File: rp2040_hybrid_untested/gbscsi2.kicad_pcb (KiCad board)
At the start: 4 copper layers, 69.5 x 93.5 mm, 143 parts, among them J1 USB_DATA, J2 TF003, J3 Conn_01x02, J4 Conn_01x04, J5 SCSI_50-2P_2mm, J6 SCSI_50P_2.54mm, J7 Conn_01x04, Q1 AO3401A, Q10 AO3401A, Q11 AO3401A, Q12 AO3401A, Q13 AO3401A, Q14 AO3401A, Q15 AO3401A, Q16 AO3401A, Q17 AO3401A, Q18 AO3401A, Q2 AO3401A, Q3 AO3401A, Q4 AO3401A, Q5 AO3401A, Q6 AO3401A, Q7 AO3401A, Q8 AO3401A, Q9 AO3401A, SW1 SW_DIP_x04, U1 RP2040, U10 W25Q128JVS, U2 74LVT245, U3 74LVT245, U4 74AHCT1G125, U5 74LVT125, U6 74LVT125, U7 AZ1117-2.85, U8 AP62250WU, U9 USB TVS, Y1 12MHz

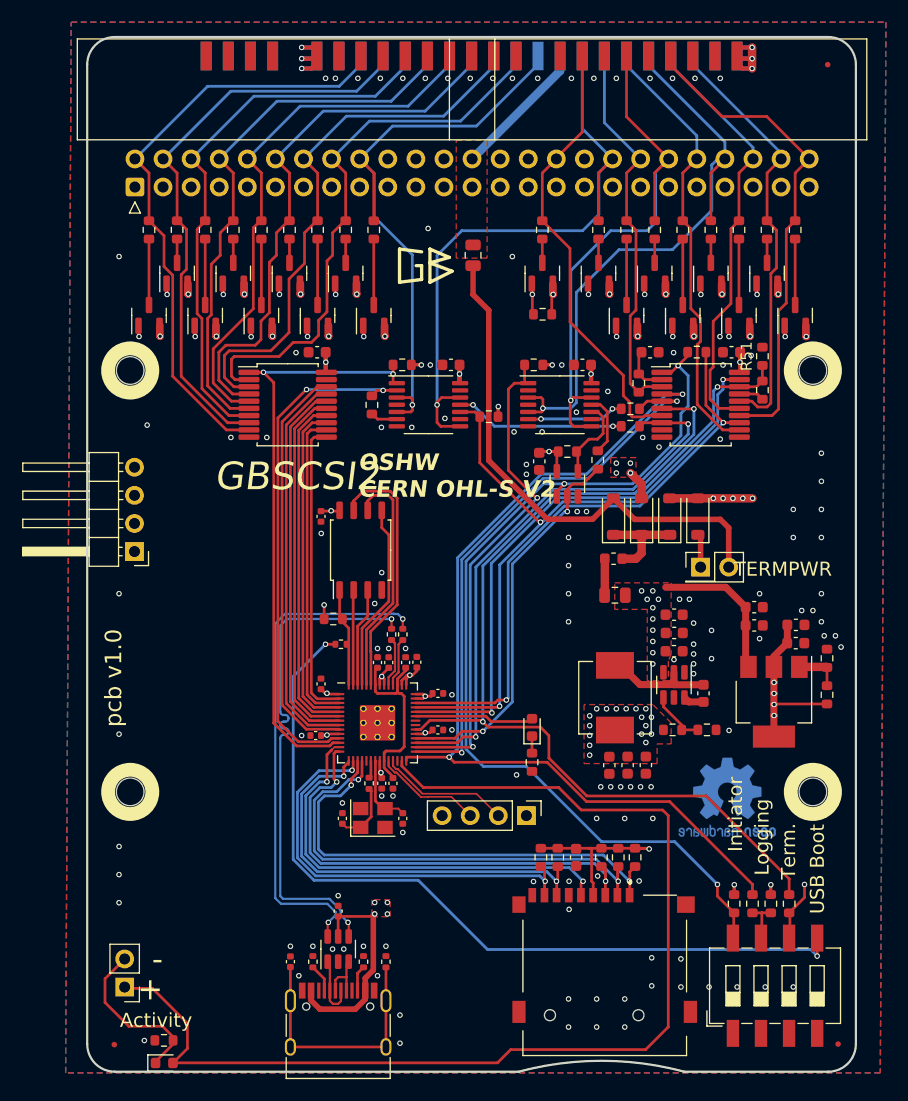
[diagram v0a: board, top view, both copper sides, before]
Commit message: Corrected wrong keying on 2.5" connector
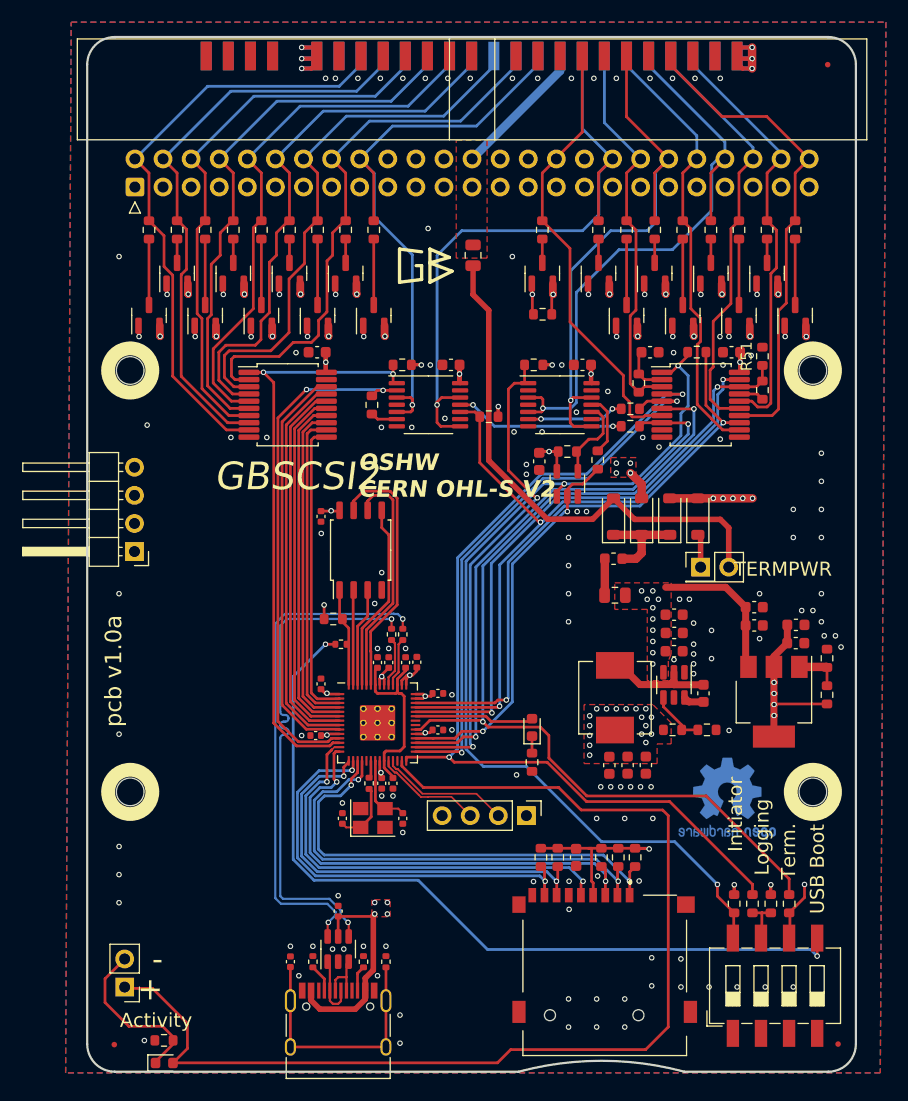
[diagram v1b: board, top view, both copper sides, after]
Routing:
- net GND: vias 134 -> 133
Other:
- board text added: "pcb v1.0a"
- board text removed: "pcb v1.0"
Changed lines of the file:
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@@
     (pad "16" smd rect (at -2.085 0 90) (size 2.58 1) (layers "B.Cu" "B.Paste" "B.Mask")
       (net 22 "/~{SCSI_SD5}") (pinfunction "Pin_16") (pintype "passive"))
-    (pad "17" smd rect (at -2.085 2 90) (size 2.58 1) (layers "F.Cu" "F.Paste" "F.Mask")
-      (net 1 "GND") (pinfunction "Pin_17") (pintype "passive"))
     (pad "18" smd rect (at -2.085 2 90) (size 2.58 1) (layers "B.Cu" "B.Paste" "B.Mask")
       (net 23 "/~{SCSI_SD6}") (pinfunction "Pin_18") (pintype "passive"))
@@
     (pad "20" smd rect (at -2.085 4 90) (size 2.58 1) (layers "B.Cu" "B.Paste" "B.Mask")
       (net 24 "/~{SCSI_SD7}") (pinfunction "Pin_20") (pintype "passive"))
+    (pad "21" smd rect (at -2.085 6 90) (size 2.58 1) (layers "F.Cu" "F.Paste" "F.Mask"))
     (pad "22" smd rect (at -2.085 6 90) (size 2.58 1) (layers "B.Cu" "B.Paste" "B.Mask")
       (net 25 "/~{SCSI_SDP}") (pinfunction "Pin_22") (pintype "passive"))
@@
   (gr_line (start 42.8 43.65) (end 107.3 43.65)
     (stroke (width 0.2) (type solid)) (layer "Edge.Cuts"))
-  (gr_text "pcb v1.0" (at 43.561 106.045 90) (layer "F.SilkS")
+  (gr_text "pcb v1.0a" (at 43.561 106.045 90) (layer "F.SilkS")
     (effects (font (face "OCR A Extended") (size 1.5 1.5) (thickness 0.15)) (justify left bottom))
-    (render_cache "pcb v1.0" 90
+    (render_cache "pcb v1.0a" 90
       (polygon
         (pts
@@
         )
       )
+      (polygon
+        (pts
+          (xy 43.235452 94.82011)          (xy 43.251515 94.824581)          (xy 43.266204 94.832303)          (xy 43.27793 94.841728)
+          (xy 43.281087 94.844877)          (xy 43.290794 94.856553)          (xy 43.298968 94.871013)          (xy 43.304029 94.886664)
+          (xy 43.305902 94.901335)          (xy 43.306 94.905694)          (xy 43.304702 94.921357)          (xy 43.30081 94.935968)
+          (xy 43.294324 94.949527)          (xy 43.285243 94.962034)          (xy 43.278889 94.968709)          (xy 43.266306 94.978701)
+          (xy 43.252602 94.98624)          (xy 43.237776 94.991324)          (xy 43.221827 94.993953)          (xy 43.21221 94.994354)
+          (xy 43.306 95.140533)          (xy 43.306 95.433258)          (xy 43.305346 95.453439)          (xy 43.303385 95.47304)
+          (xy 43.300117 95.492062)          (xy 43.295541 95.510504)          (xy 43.289658 95.528366)          (xy 43.282468 95.545649)
+          (xy 43.27397 95.562352)          (xy 43.264165 95.578476)          (xy 43.253053 95.59402)          (xy 43.240634 95.608984)
+          (xy 43.231628 95.618639)          (xy 43.217399 95.632257)          (xy 43.202605 95.644536)          (xy 43.187243 95.655476)
+          (xy 43.171315 95.665075)          (xy 43.15482 95.673336)          (xy 43.137758 95.680257)          (xy 43.12013 95.685838)
+          (xy 43.101935 95.69008)          (xy 43.083173 95.692982)          (xy 43.063844 95.694545)          (xy 43.050644 95.694842)
+          (xy 42.951725 95.694842)          (xy 42.932212 95.69417)          (xy 42.91324 95.692151)          (xy 42.894809 95.688786)
+          (xy 42.876918 95.684075)          (xy 42.859569 95.678018)          (xy 42.842761 95.670615)          (xy 42.826493 95.661866)
+          (xy 42.810767 95.651772)          (xy 42.795581 95.640331)          (xy 42.780937 95.627545)          (xy 42.771474 95.618272)
+          (xy 42.758052 95.603573)          (xy 42.74595 95.588326)          (xy 42.735169 95.572532)          (xy 42.725707 95.556191)
+          (xy 42.717566 95.539302)          (xy 42.710745 95.521866)          (xy 42.705244 95.503882)          (xy 42.701063 95.485351)
+          (xy 42.698203 95.466272)          (xy 42.696663 95.446646)          (xy 42.696369 95.433258)          (xy 42.860501 95.433258)
+          (xy 42.861763 95.448458)          (xy 42.86555 95.462641)          (xy 42.872968 95.477604)          (xy 42.882165 95.489608)
+          (xy 42.886879 95.494441)          (xy 42.898945 95.504291)          (xy 42.912063 95.511722)          (xy 42.926234 95.516733)
+          (xy 42.941456 95.519325)          (xy 42.950626 95.51972)          (xy 43.051743 95.51972)          (xy 43.067173 95.518493)
+          (xy 43.081726 95.514812)          (xy 43.095403 95.508676)          (xy 43.108203 95.500086)          (xy 43.115124 95.494075)
+          (xy 43.125545 95.482274)          (xy 43.133406 95.469632)          (xy 43.139257 95.454153)          (xy 43.141764 95.437575)
+          (xy 43.141868 95.433258)          (xy 43.141868 95.188893)          (xy 43.048079 95.000216)          (xy 42.961983 95.005345)
+          (xy 42.946274 95.006594)          (xy 42.931569 95.009518)          (xy 42.915684 95.015045)          (xy 42.901166 95.022852)
+          (xy 42.88981 95.031357)          (xy 42.878389 95.042639)          (xy 42.869774 95.055009)          (xy 42.863964 95.068465)
+          (xy 42.860959 95.083008)          (xy 42.860501 95.091807)          (xy 42.860501 95.433258)          (xy 42.696369 95.433258)
+          (xy 42.696369 95.094005)          (xy 42.696209 95.078549)          (xy 42.695806 95.062508)          (xy 42.695265 95.046889)
+          (xy 42.694544 95.029544)          (xy 42.693805 95.013771)          (xy 42.571439 95.015969)          (xy 42.556257 95.017179)
+          (xy 42.540194 95.021524)          (xy 42.525506 95.029029)          (xy 42.51378 95.038187)          (xy 42.510623 95.041249)
+          (xy 42.500773 95.052817)          (xy 42.492478 95.067282)          (xy 42.487343 95.083076)          (xy 42.485442 95.097985)
+          (xy 42.485344 95.102431)          (xy 42.485344 95.43106)          (xy 42.484186 95.445866)          (xy 42.480031 95.461758)
+          (xy 42.472852 95.476549)          (xy 42.464092 95.488591)          (xy 42.461163 95.491877)          (xy 42.450004 95.501869)
+          (xy 42.436219 95.510284)          (xy 42.421336 95.515494)          (xy 42.405353 95.517497)          (xy 42.403278 95.517522)
+          (xy 42.386883 95.515942)          (xy 42.371771 95.511202)          (xy 42.35794 95.503303)          (xy 42.345392 95.492243)
+          (xy 42.335971 95.480675)          (xy 42.328037 95.466209)          (xy 42.323125 95.450416)          (xy 42.321307 95.435507)
+          (xy 42.321212 95.43106)          (xy 42.321212 95.102065)          (xy 42.321869 95.08228)          (xy 42.32384 95.063043)
+          (xy 42.327124 95.044353)          (xy 42.331722 95.026211)          (xy 42.337634 95.008615)          (xy 42.34486 94.991568)
+          (xy 42.353399 94.975067)          (xy 42.363253 94.959114)          (xy 42.37442 94.943709)          (xy 42.3869 94.928851)
+          (xy 42.395951 94.919249)          (xy 42.410192 94.905671)          (xy 42.425025 94.893373)          (xy 42.440451 94.882358)
+          (xy 42.456469 94.872624)          (xy 42.47308 94.864171)          (xy 42.490284 94.857)          (xy 42.50808 94.851111)
+          (xy 42.526468 94.846503)          (xy 42.545449 94.843177)          (xy 42.565022 94.841132)          (xy 42.5784 94.840481)
+          (xy 43.22027 94.818866)
+        )
+      )
     )
   )
@@
   (via (at 83.82 96.52) (size 0.5) (drill 0.3) (layers "F.Cu" "B.Cu") (free) (net 1))
   (via (at 107.95 97.79) (size 0.5) (drill 0.3) (layers "F.Cu" "B.Cu") (free) (net 1))
-  (via (at 76.966 47.384) (size 0.5) (drill 0.3) (layers "F.Cu" "B.Cu") (free) (net 1))
   (via (at 70.87 47.384) (size 0.5) (drill 0.3) (layers "F.Cu" "B.Cu") (free) (net 1))
   (via (at 83.82 91.44) (size 0.5) (drill 0.3) (layers "F.Cu" "B.Cu") (free) (net 1))

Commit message: Changed diodes in BoM, minor corrections to PCB, documentation
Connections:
- J5 pad 21: (no net) -> GND
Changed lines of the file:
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@@
     (descr "SOD-123")
     (tags "SOD-123")
-    (property "LCSC" "C8598")
+    (property "LCSC" "C82544")
     (property "Sheetfile" "gbscsi2.kicad_sch")
     (property "Sheetname" "")
@@
     (descr "SOD-123")
     (tags "SOD-123")
-    (property "LCSC" "C8598")
+    (property "LCSC" "C82544")
     (property "Sheetfile" "gbscsi2.kicad_sch")
     (property "Sheetname" "")
@@
     (descr "SOD-123")
     (tags "SOD-123")
-    (property "LCSC" "C8598")
+    (property "LCSC" "C82544")
     (property "Sheetfile" "gbscsi2.kicad_sch")
     (property "Sheetname" "")
@@
     (pad "20" smd rect (at -2.085 4 90) (size 2.58 1) (layers "B.Cu" "B.Paste" "B.Mask")
       (net 24 "/~{SCSI_SD7}") (pinfunction "Pin_20") (pintype "passive"))
-    (pad "21" smd rect (at -2.085 6 90) (size 2.58 1) (layers "F.Cu" "F.Paste" "F.Mask"))
+    (pad "21" smd rect (at -2.085 6 90) (size 2.58 1) (layers "F.Cu" "F.Paste" "F.Mask")
+      (net 1 "GND") (pinfunction "Pin_21") (pintype "passive"))
     (pad "22" smd rect (at -2.085 6 90) (size 2.58 1) (layers "B.Cu" "B.Paste" "B.Mask")
       (net 25 "/~{SCSI_SDP}") (pinfunction "Pin_22") (pintype "passive"))
@@
     (descr "SOD-123")
     (tags "SOD-123")
-    (property "LCSC" "C8598")
+    (property "LCSC" "C82544")
     (property "Sheetfile" "gbscsi2.kicad_sch")
     (property "Sheetname" "")
